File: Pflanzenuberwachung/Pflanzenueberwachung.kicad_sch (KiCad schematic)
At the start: 0 parts

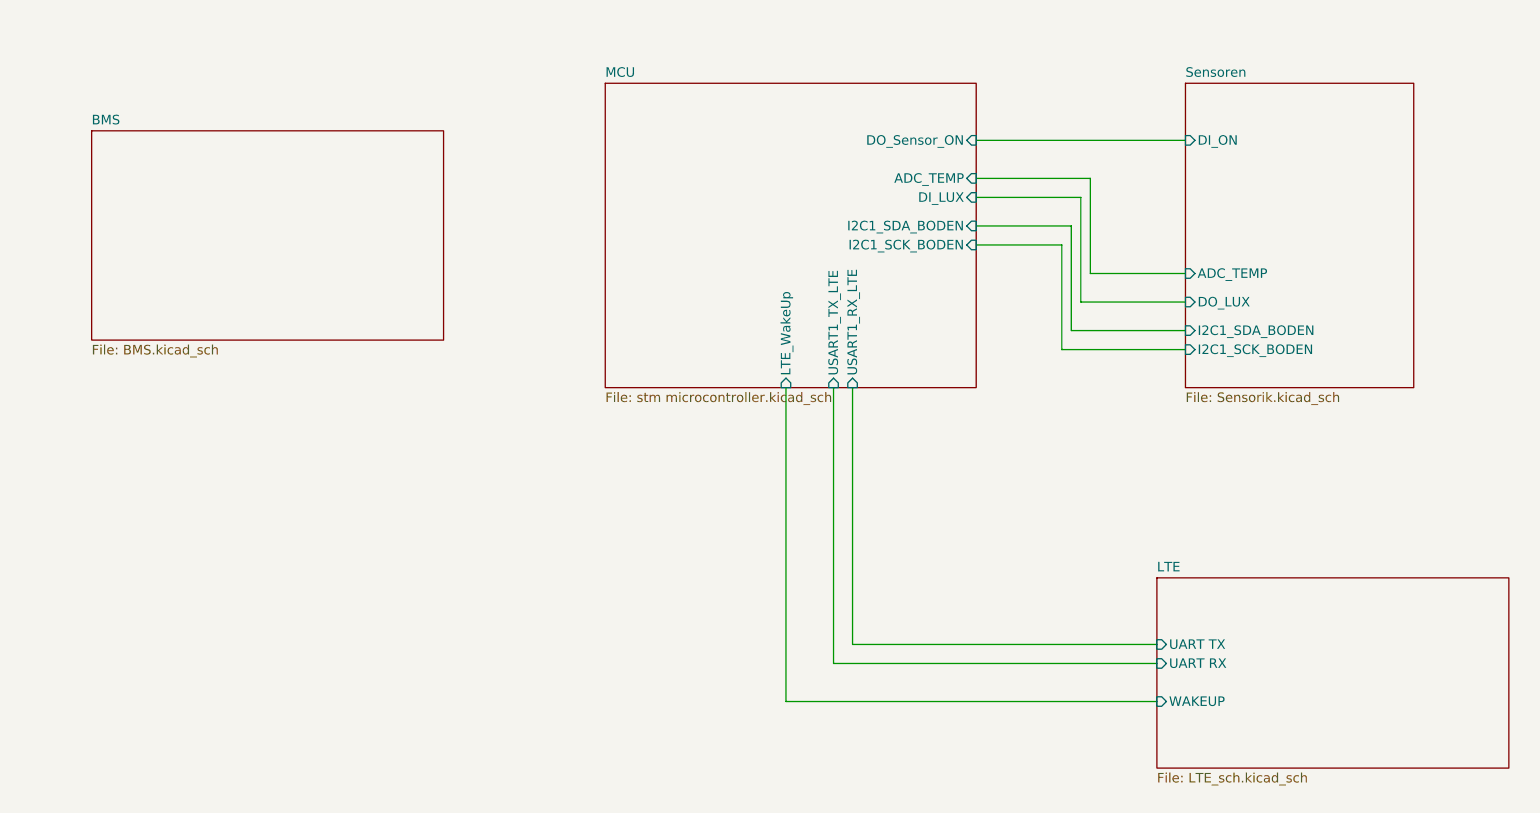
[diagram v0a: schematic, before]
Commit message: PCB Bord
PCB Design und kleiner nicht relevante änderungen
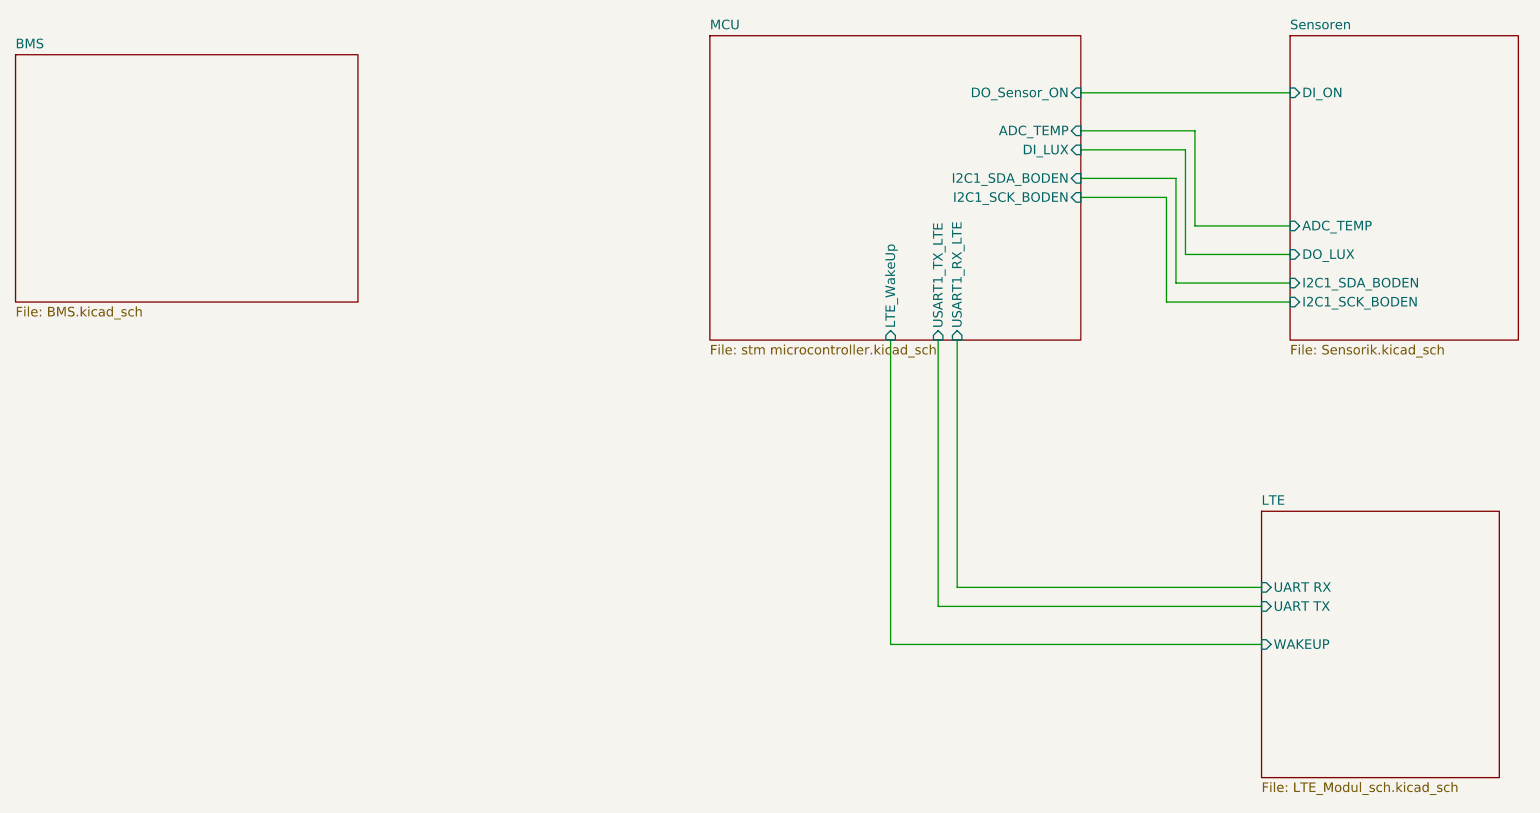
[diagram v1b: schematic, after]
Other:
- sheet LTE: file LTE_sch.kicad_sch -> LTE_Modul_sch.kicad_sch
